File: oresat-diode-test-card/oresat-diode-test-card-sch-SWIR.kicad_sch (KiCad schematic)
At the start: 22 parts, among them Q3 NMOS, Q4 DMP3050LVT-7, U4 TLV6001DCK, U501 TLV6001DCK, U8 NX3L4051-Q100, U9 TLV6001DCK

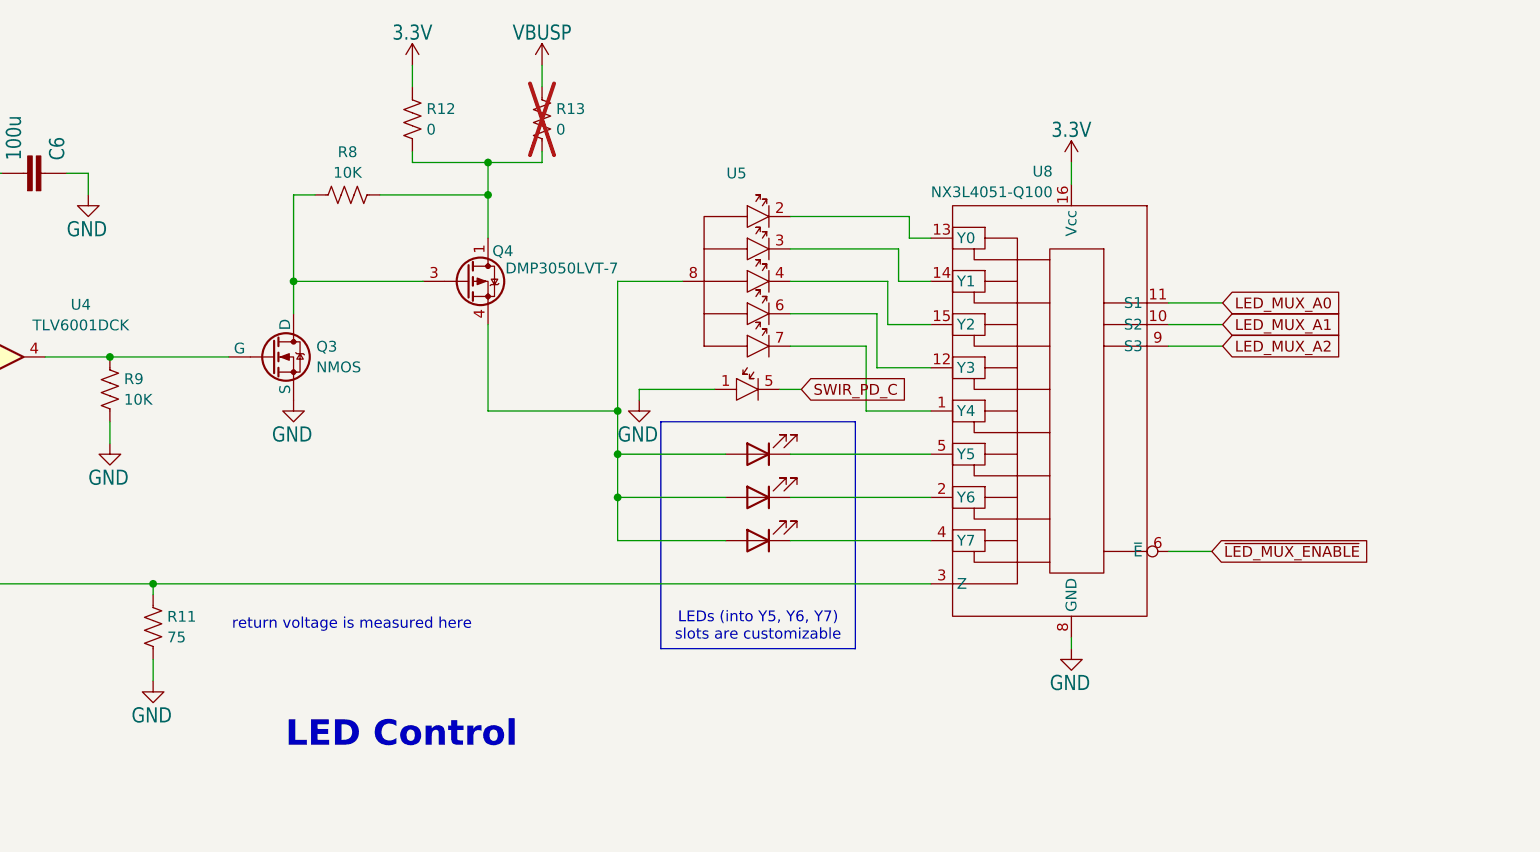
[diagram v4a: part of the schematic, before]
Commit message: started layout of components
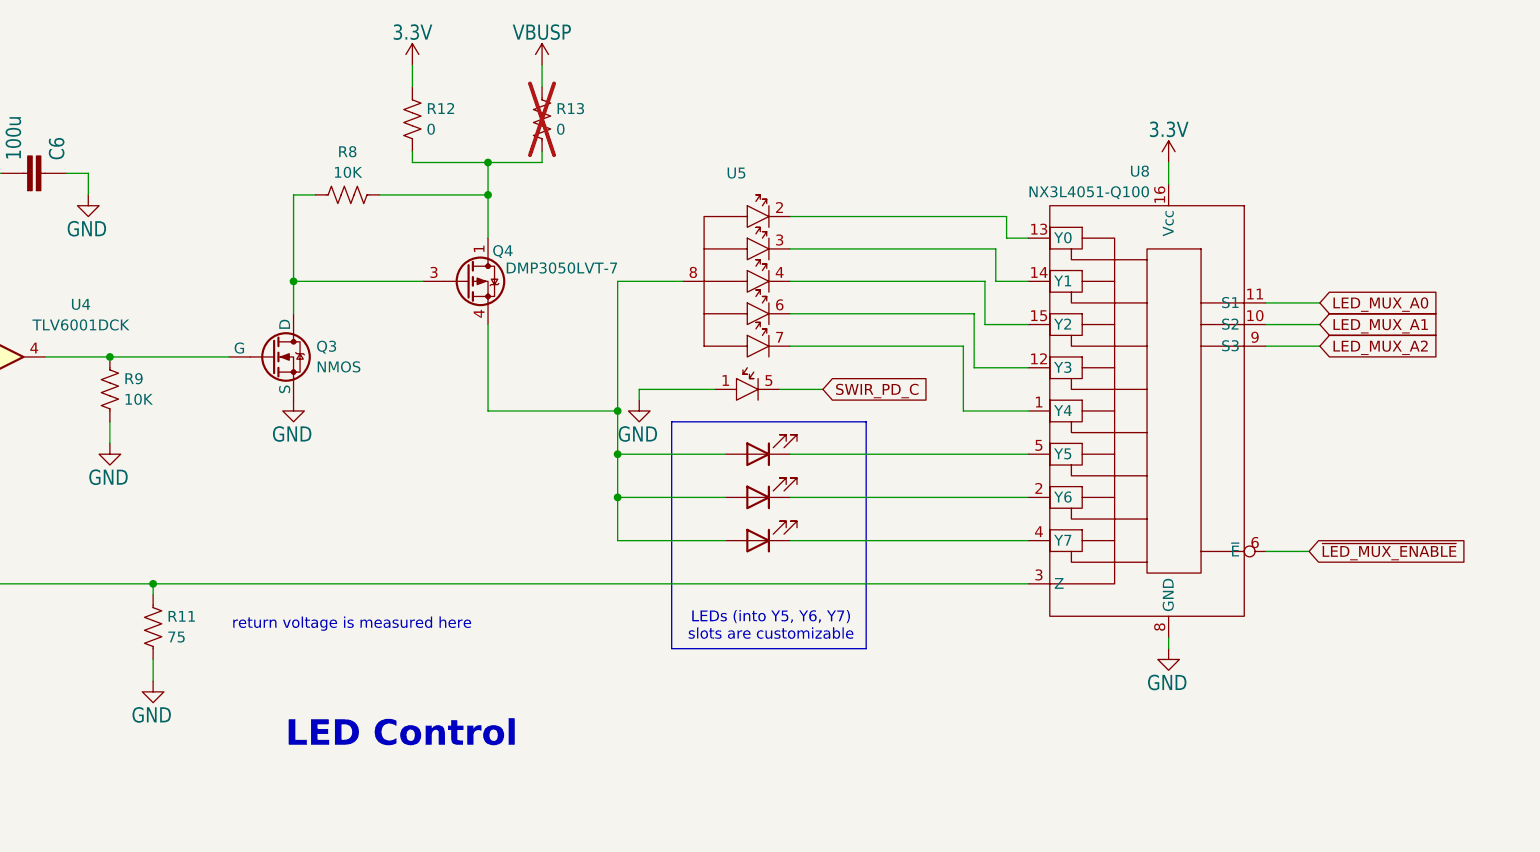
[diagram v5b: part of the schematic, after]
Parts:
- D1, D2, D4: footprint (none) -> oresat-diodes:LED_0603_1608Metric
- Q3: footprint (none) -> Package_TO_SOT_SMD:SOT-23-6
- R10, R11, R12, R13, R14, R501, R8, R9: footprint (none) -> oresat-passives:0603-C-NOSILK
- U5: footprint Diode_THT:SWIR_PhotoDiode -> oresat-diodes:MTMD142345PDT38
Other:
- moved on the sheet: U8

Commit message: intial layout placed
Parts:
- added HW1, HW2, HW3, HW4, HW5, HW6, HW7, HW8: M2-Press-Fit-Nut, oresat-misc:M2-Press-Fit-Nut, symbol oresat-misc:M2-Press-Fit-Nut
- D1, D2, D4: footprint oresat-diodes:LED_0603_1608Metric -> Diode_SMD:D_0201_0603Metric
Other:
- note added: "Fastner Holes for Diode Cover"

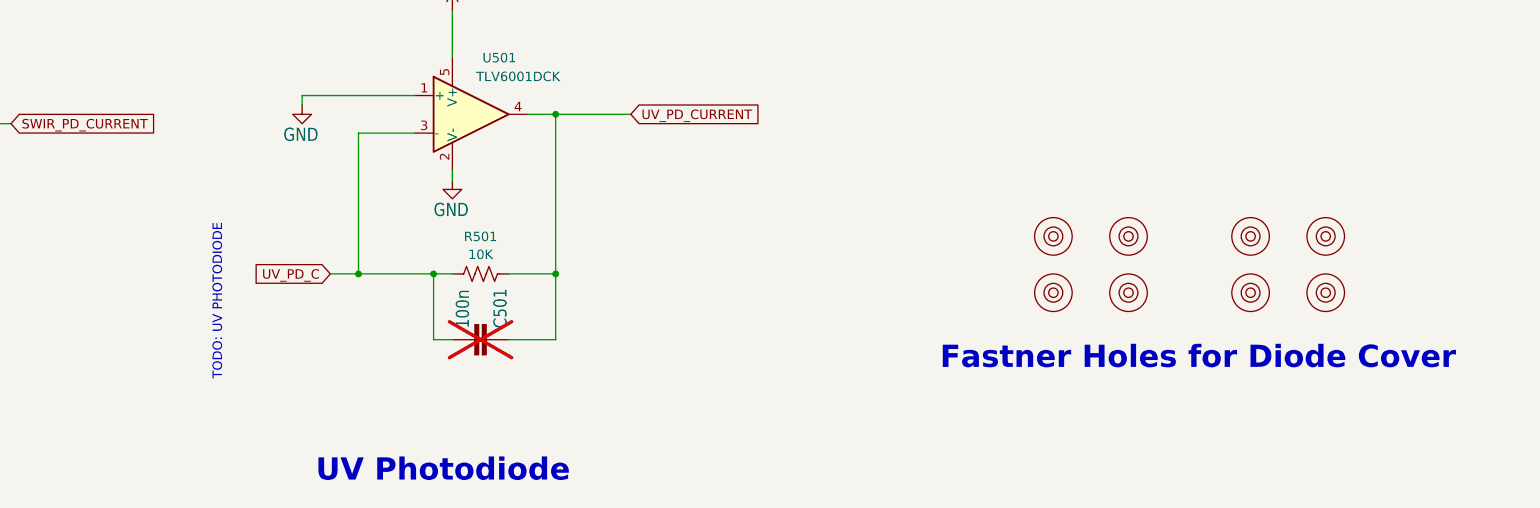
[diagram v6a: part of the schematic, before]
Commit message: updated UV LED package type
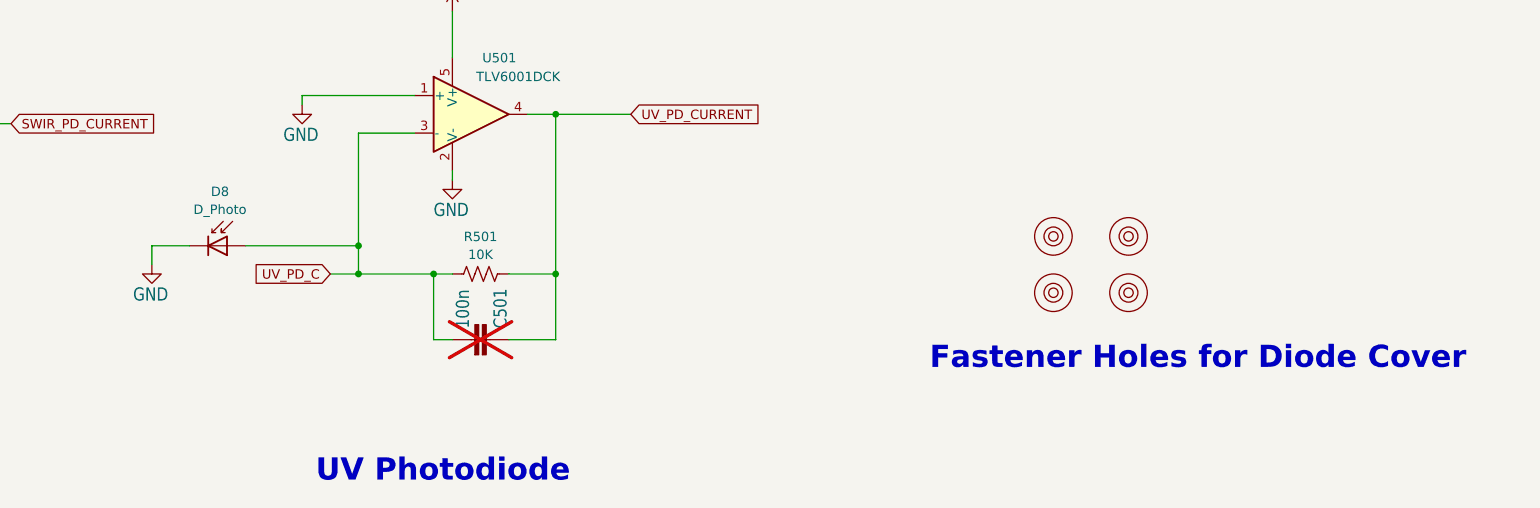
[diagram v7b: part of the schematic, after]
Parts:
- removed HW5, HW6, HW7, HW8: M2-Press-Fit-Nut, oresat-misc:M2-Press-Fit-Nut, symbol oresat-misc:M2-Press-Fit-Nut
- added D8: D_Photo, oresat-diodes:GVBL-S12SD, symbol Device:D_Photo
- D1, D2, D4: footprint Diode_SMD:D_0201_0603Metric -> Package_TO_SOT_THT:TO-92-2
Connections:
- net GND: now also D8.1 (K)
- net UV_PD_C: now also D8.2 (A)
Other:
- note added: "Fastener Holes for Diode Cover"
- note removed: "Fastner Holes for Diode Cover"
- note removed: "TODO: UV PHOTODIODE"

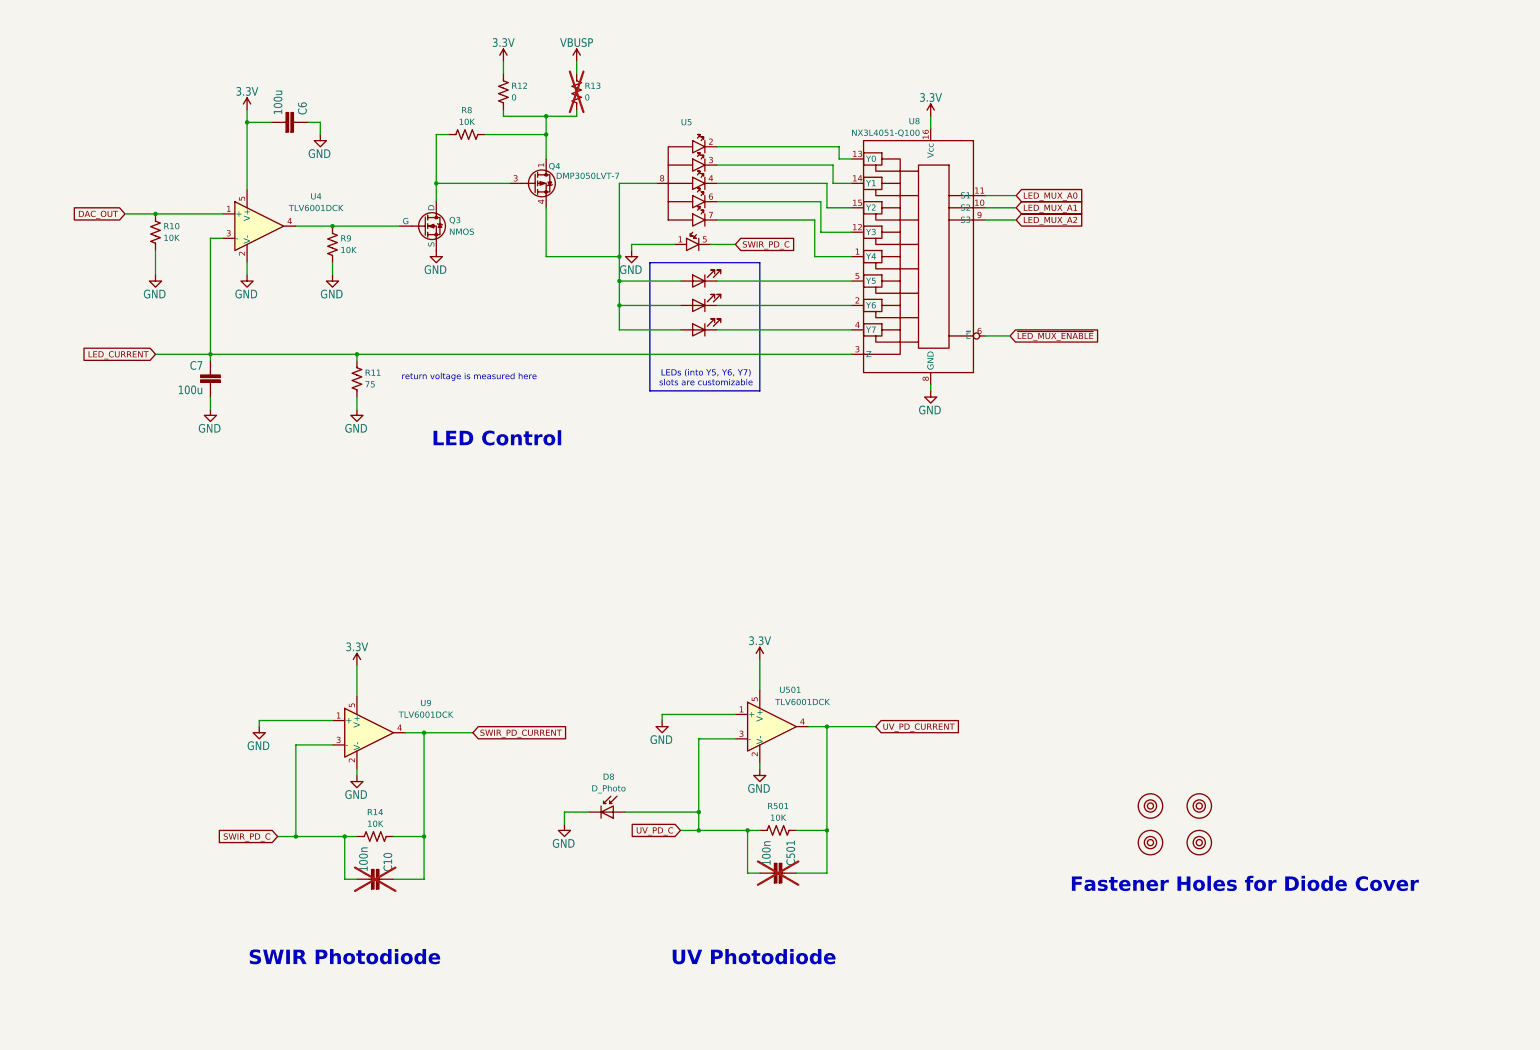
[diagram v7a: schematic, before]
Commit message: updated layout and schematic with correct values
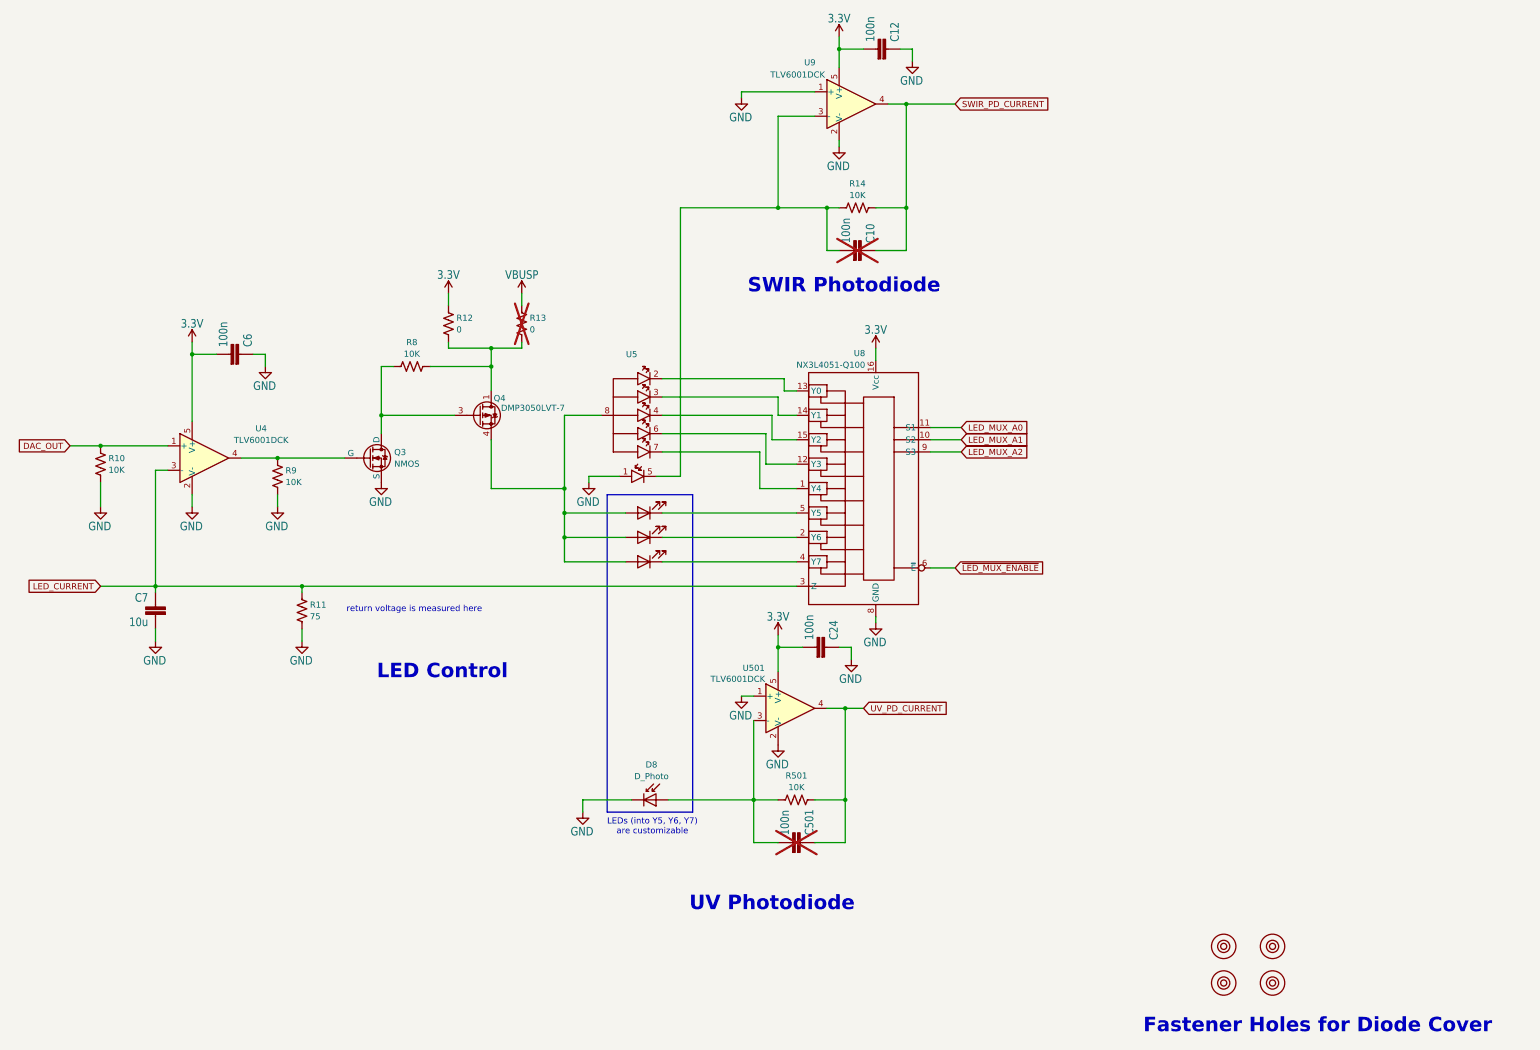
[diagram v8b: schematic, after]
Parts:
- added C12, C24: 100n, oresat-passives:0603-C-NOSILK, symbol oresat-proto-card-eagle-import:C-EU0603-C-NOSILK
- C6: value 100u -> 100n
- C7: value 100u -> 10u
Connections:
- net 3.3V: now also C12.2, C24.2
- net GND: now also C12.1, C24.1
- net SWIR_PD_C: no longer names the net of C10.2, R14.1, U5.5 (PD_Cathode), U9.3 (-)
- net UV_PD_C: no longer names the net of C501.2, D8.2 (A), R501.1, U501.3 (-)
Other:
- note added: "LEDs (into Y5, Y6, Y7) are customizable"
- note removed: "LEDs (into Y5, Y6, Y7) slots are customizable"
- moved on the sheet: C10, C501, C6, C7, D8, Q3, Q4, R10, R11, R12, R13, R14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
